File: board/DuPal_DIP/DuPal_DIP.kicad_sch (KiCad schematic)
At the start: 55 parts, among them J1 AVR-ISP-6, J2 RS232, J3 Power IN, SW1 SW_Push, SW2 Power, U1 ATmega8A-PU, U10 24 Pin PAL, U2 74HC595, U3 74HC595, U5 20 Pin PAL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

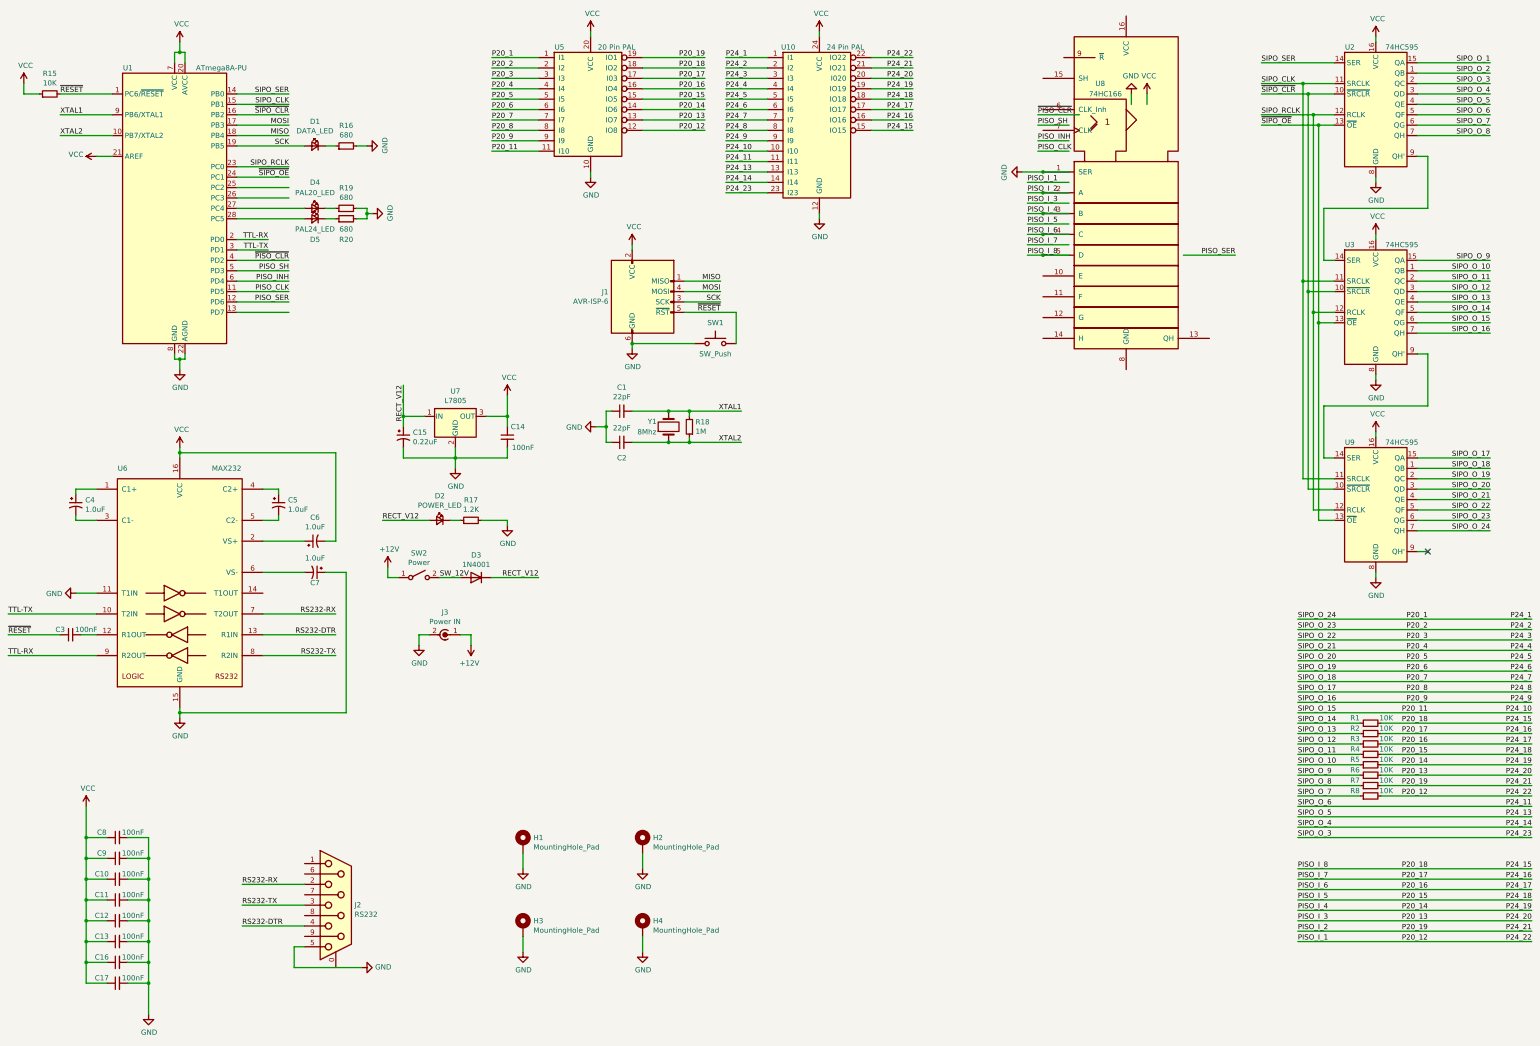
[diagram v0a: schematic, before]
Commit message: Fixes schematics
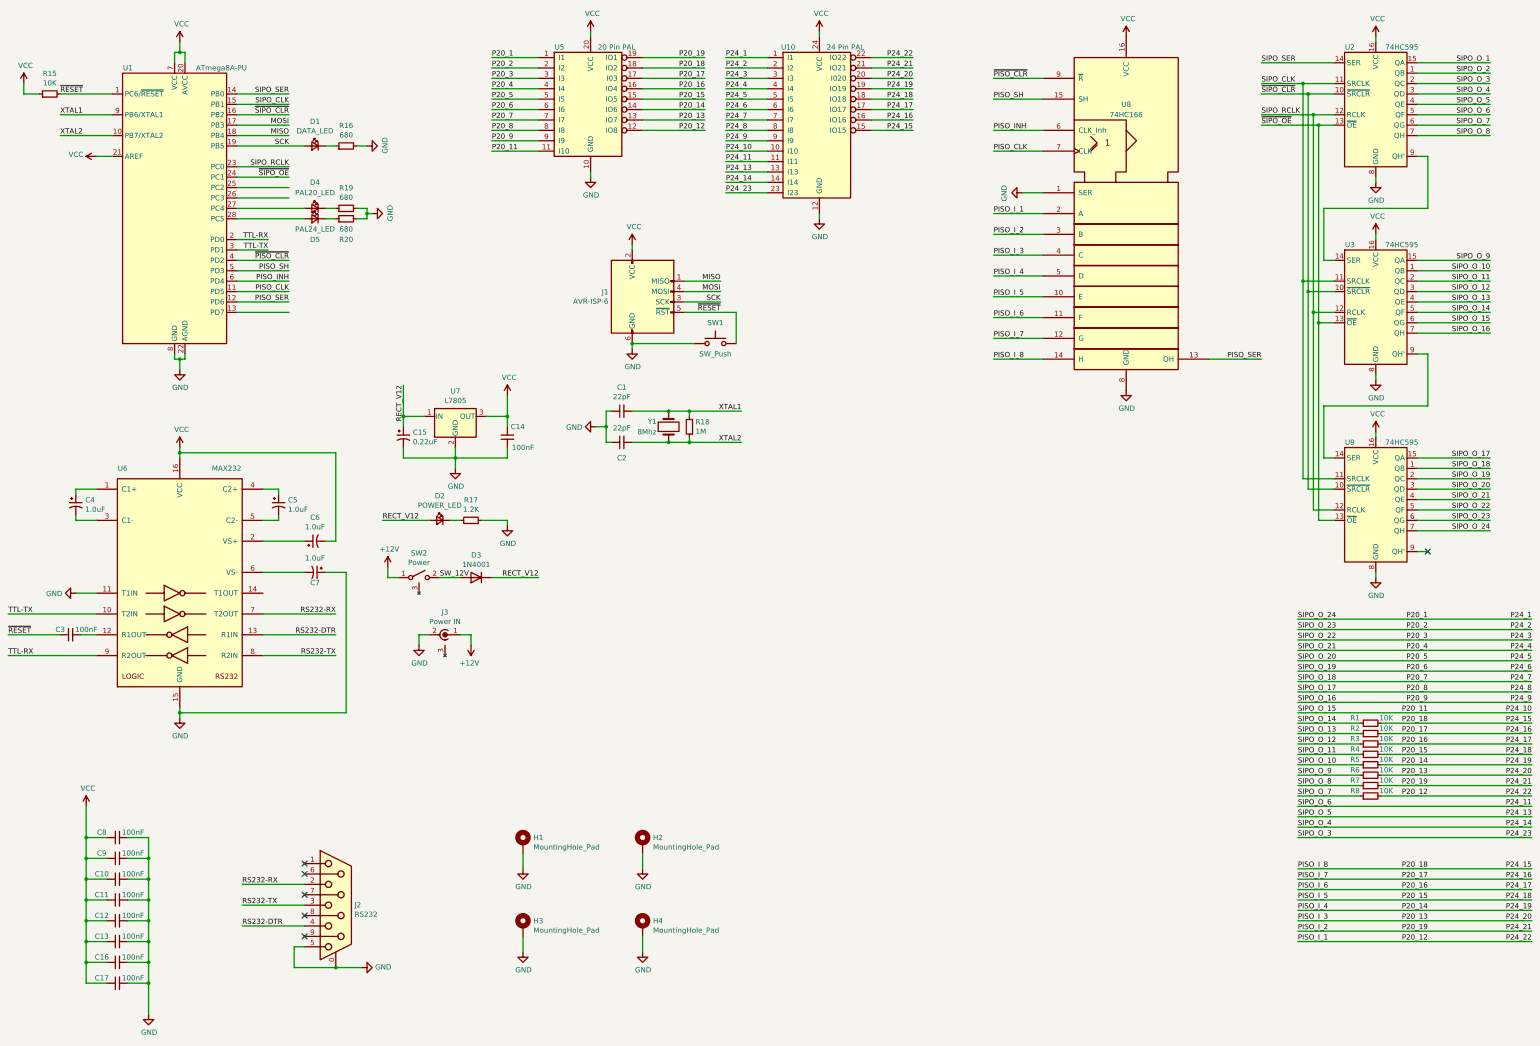
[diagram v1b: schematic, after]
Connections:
- net GND: now also J2.0 (PAD), U8.8 (GND)
- net P20_12: now also U8.2 (A)
- net P20_13: now also U8.4 (C)
- net P20_14: now also U8.5 (D); no longer U8.3 (B)
- net P20_15: now also U8.10 (E)
- net P20_16: now also U8.11 (F); no longer U8.4 (C)
- net P20_17: now also U8.12 (G)
- net P20_18: now also U8.14 (H); no longer U8.5 (D)
- net P20_19: now also U8.3 (B); no longer U8.2 (A)
- net PISO_CLK: now also U8.7 (CLK)
- net PISO_INH: now also U8.6 (CLK_Inh)
- net PISO_SER: now also U8.13 (QH)
- net PISO_SH: now also U8.15 (SH)
- net VCC: now also U8.16 (VCC)
- net ~{PISO_CLR}: now also U8.9 (~{R})
- no-connect marks 1 -> 6
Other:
- moved on the sheet: U8

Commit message: Resolves ERC issues
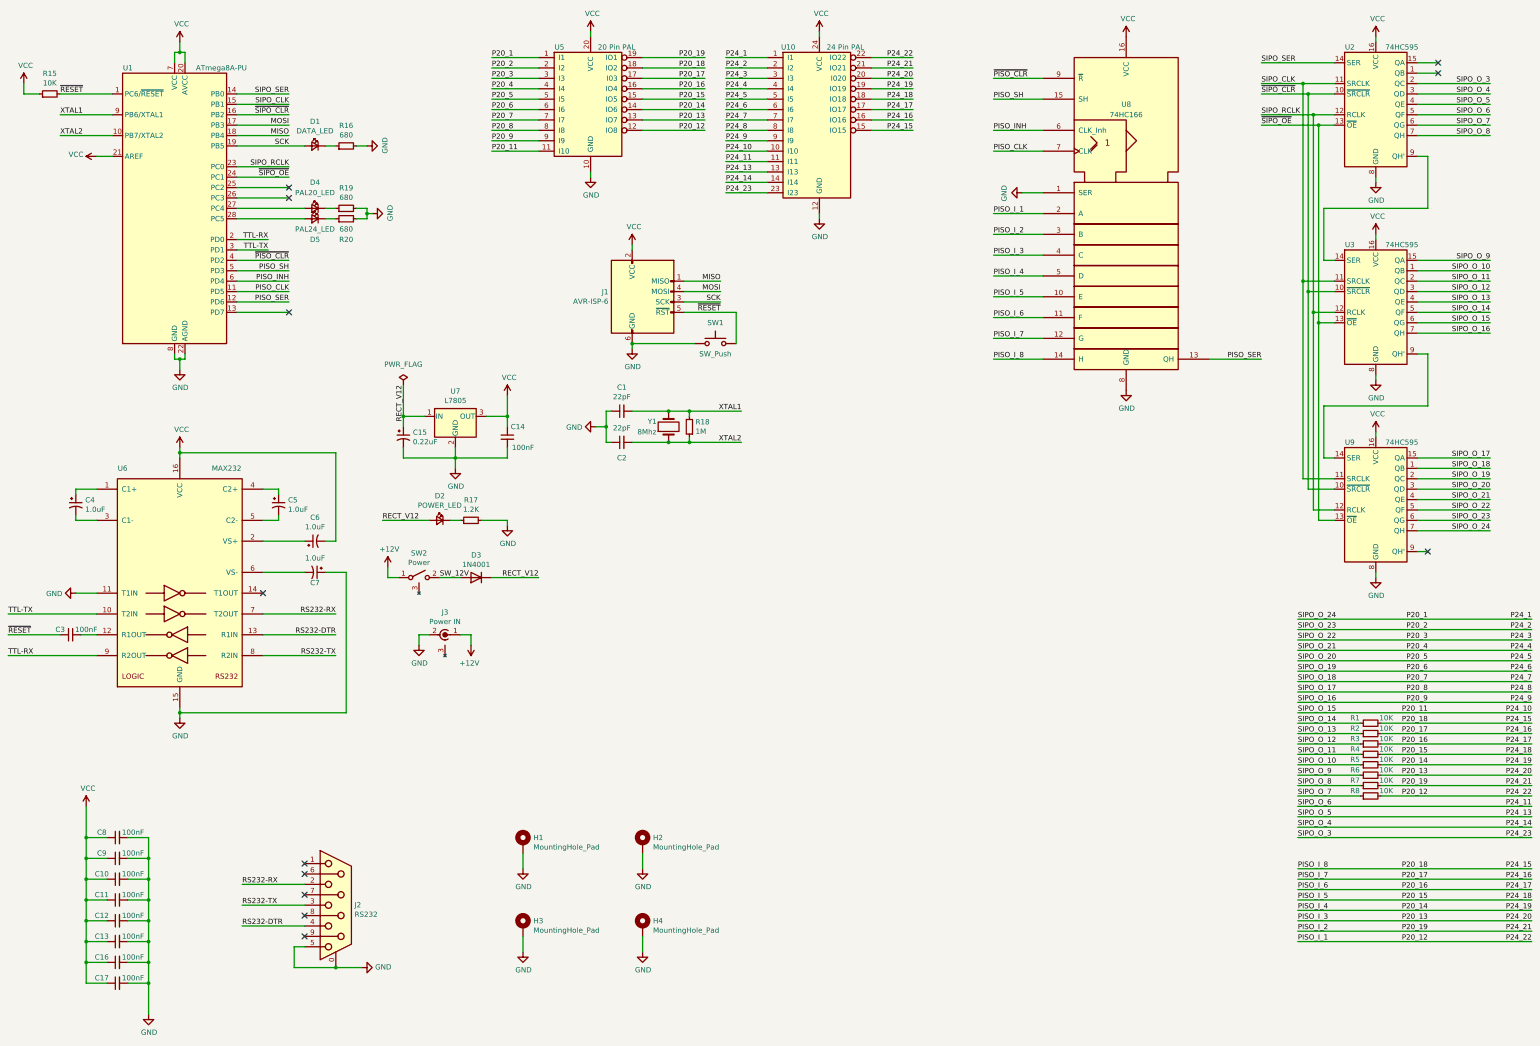
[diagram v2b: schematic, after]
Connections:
- net SIPO_O_1: no longer names the net of U2.15 (QA)
- net SIPO_O_2: no longer names the net of U2.1 (QB)
- no-connect marks 6 -> 12
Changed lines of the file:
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@@
   )
   (no_connect (at 90.17 241.3))
+  (no_connect (at 86.36 88.9))
+  (no_connect (at 86.36 60.96))
+  (no_connect (at 367.03 27.94))
   (no_connect (at 90.17 226.06))
+  (no_connect (at 367.03 30.48))
   (no_connect (at 90.17 223.52))
+  (no_connect (at 80.01 157.48))
+  (no_connect (at 86.36 58.42))
   (no_connect (at 90.17 231.14))
   (no_connect (at 90.17 236.22))
@@
     (stroke (width 0) (type default))
   )
+  (wire (pts (xy 367.03 27.94) (xy 361.95 27.94))
+    (stroke (width 0) (type default))
+  )
   (wire (pts (xy 97.79 48.26) (xy 95.25 48.26))
     (stroke (width 0) (type default))
@@
     (stroke (width 0) (type default))
   )
-  (wire (pts (xy 361.95 30.48) (xy 379.73 30.48))
-    (stroke (width 0) (type default))
-  )
   (wire (pts (xy 334.01 129.54) (xy 341.63 129.54))
     (stroke (width 0) (type default))
@@
     (stroke (width 0) (type default))
   )
-  (wire (pts (xy 361.95 27.94) (xy 379.73 27.94))
-    (stroke (width 0) (type default))
-  )
   (wire (pts (xy 73.66 71.12) (xy 81.28 71.12))
     (stroke (width 0) (type default))
@@
     (stroke (width 0) (type default))
   )
+  (wire (pts (xy 367.03 30.48) (xy 361.95 30.48))
+    (stroke (width 0) (type default))
+  )
   (wire (pts (xy 353.06 194.31) (xy 389.89 194.31))
     (stroke (width 0) (type default))
@@
     (effects (font (size 1.27 1.27)) (justify left bottom))
   )
-  (label "SIPO_O_2" (at 379.73 30.48 180) (fields_autoplaced)
-    (effects (font (size 1.27 1.27)) (justify right bottom))
-  )
   (label "P24_15" (at 389.89 224.79 180) (fields_autoplaced)
     (effects (font (size 1.27 1.27)) (justify right bottom))
@@
     (effects (font (size 1.27 1.27)) (justify right bottom))
   )
-  (label "SIPO_O_1" (at 379.73 27.94 180) (fields_autoplaced)
-    (effects (font (size 1.27 1.27)) (justify right bottom))
-  )
   (label "PISO_I_5" (at 258.445 85.09 0) (fields_autoplaced)
     (effects (font (size 1.27 1.27)) (justify left bottom))
@@
         )
       )
+    )
+  )
+  (symbol (lib_id "power:PWR_FLAG") (at 114.3 106.68 0) (unit 1)
+    (in_bom yes) (on_board yes) (dnp no) (fields_autoplaced)
+    (property "Reference" "#FLG03" (at 114.3 104.775 0)
+      (effects (font (size 1.27 1.27)) hide)
+    )
+    (property "Value" "PWR_FLAG" (at 114.3 101.6 0)
+      (effects (font (size 1.27 1.27)))
+    )
+    (property "Footprint" "" (at 114.3 106.68 0)
+      (effects (font (size 1.27 1.27)) hide)
+    )
+    (property "Datasheet" "~" (at 114.3 106.68 0)
+      (effects (font (size 1.27 1.27)) hide)
+    )
+    (pin "1")
+    (instances
+      (project "DuPal_DIP"
+        (path "/d9a13938-7871-4b95-bbc2-db543ac3cca1"
+          (reference "#FLG03") (unit 1)
+        )
+      )

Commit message: Resolves DRC issues
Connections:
- net SIPO_O_2: now reaches U2.1 (QB)
- net SIPO_O_1: now reaches U2.15 (QA)

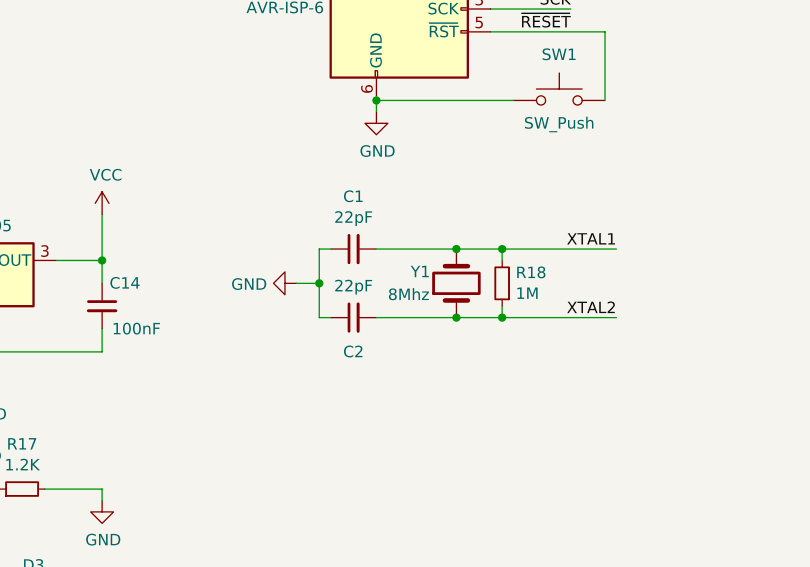
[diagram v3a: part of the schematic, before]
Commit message: Fixes crystal value
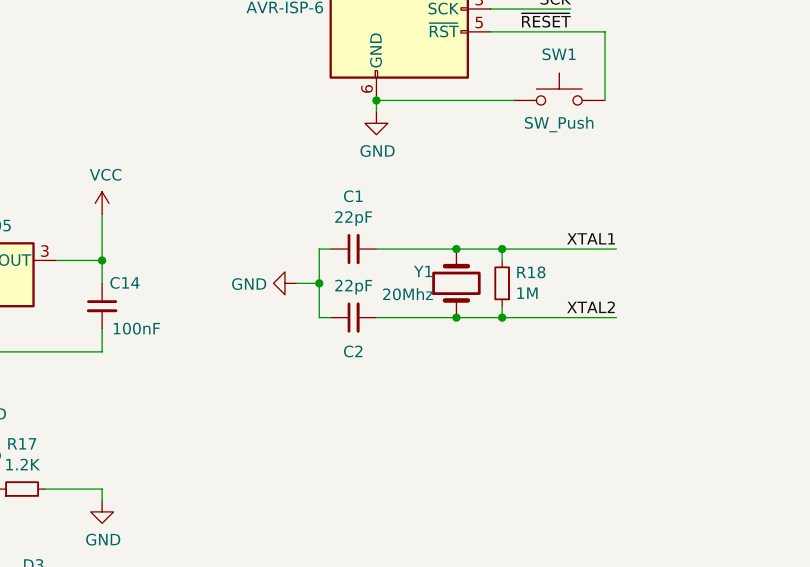
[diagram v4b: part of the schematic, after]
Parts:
- Y1: value 8Mhz -> 20Mhz
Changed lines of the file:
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@@
   (symbol (lib_id "Device:Crystal") (at 179.07 116.84 90) (unit 1)
     (in_bom yes) (on_board yes) (dnp no)
-    (property "Reference" "Y1" (at 173.99 115.57 90)
-      (effects (font (size 1.27 1.27)) (justify right))
+    (property "Reference" "Y1" (at 176.53 115.57 90)
+      (effects (font (size 1.27 1.27)) (justify left))
     )
-    (property "Value" "8Mhz" (at 171.45 118.11 90)
-      (effects (font (size 1.27 1.27)) (justify right))
+    (property "Value" "20Mhz" (at 176.53 118.11 90)
+      (effects (font (size 1.27 1.27)) (justify left))
     )
     (property "Footprint" "Crystal:Crystal_HC49-U_Vertical" (at 179.07 116.84 0)

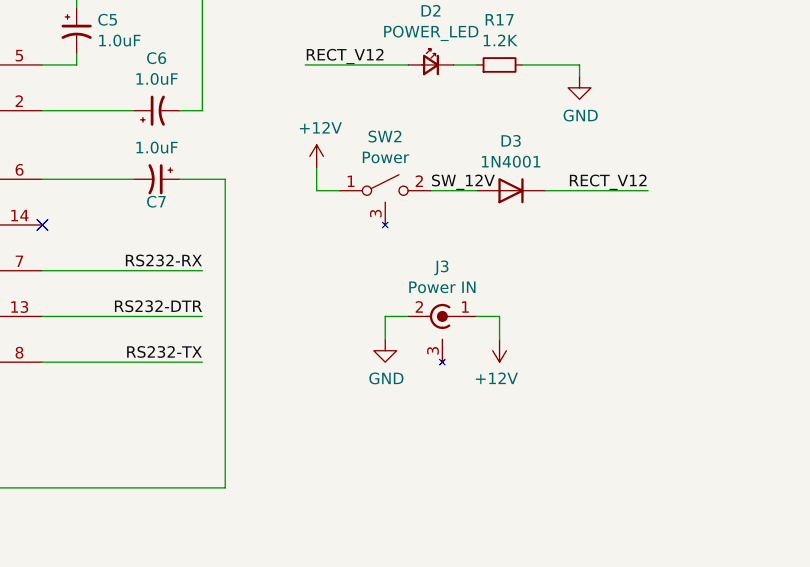
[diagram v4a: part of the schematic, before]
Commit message: Hides unconnected pins
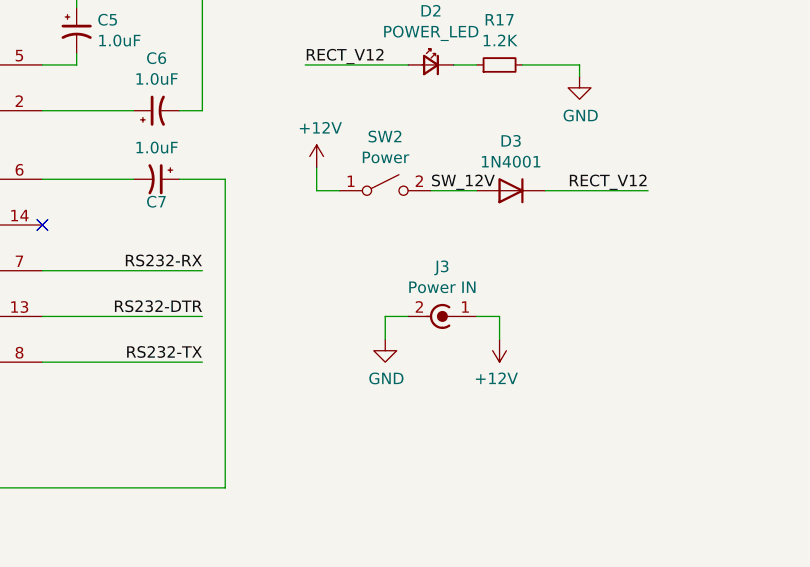
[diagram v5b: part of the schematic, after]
